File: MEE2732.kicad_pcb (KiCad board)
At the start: 2 copper layers, 16.6 x 32.9 mm, 6 parts, among them J1 Molex 78805 socket 27C32 pino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, SW1 SW_SPDT, U1 28C64

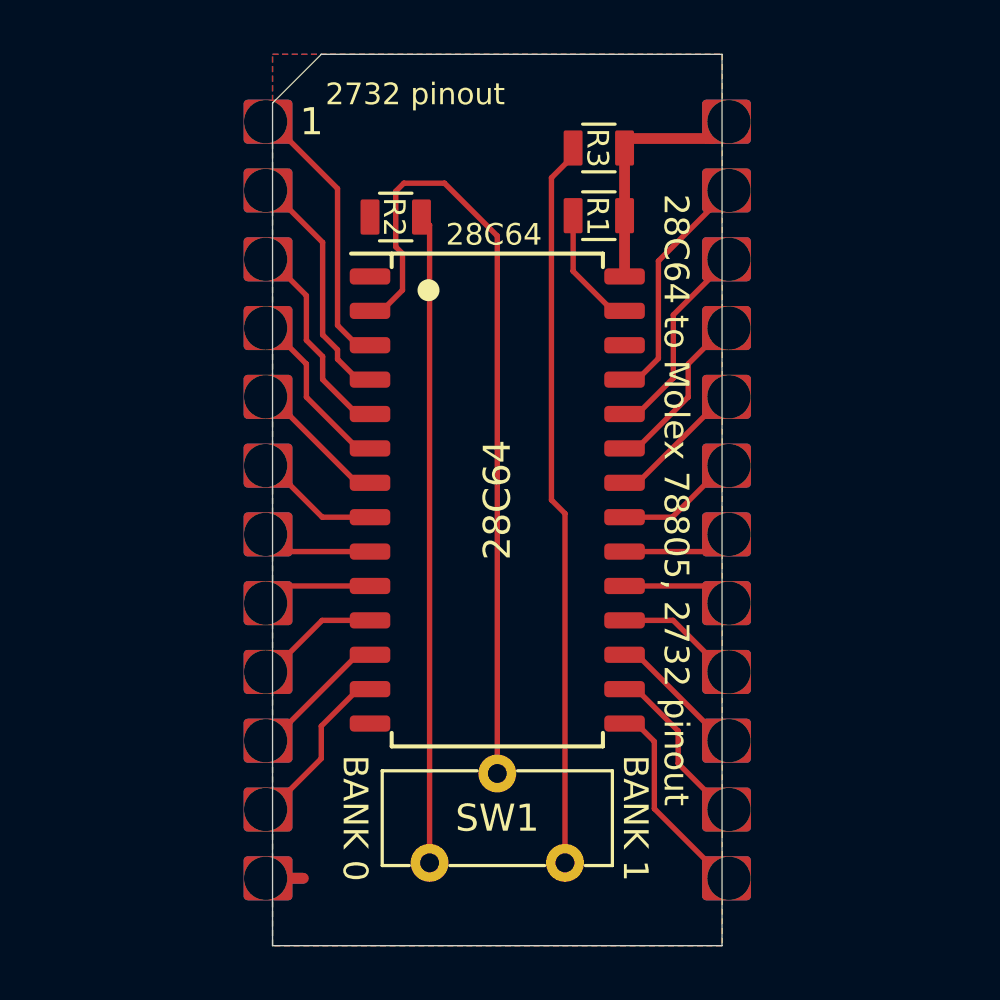
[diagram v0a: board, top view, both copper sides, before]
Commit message: kicad 6, flashopt100 programming socket
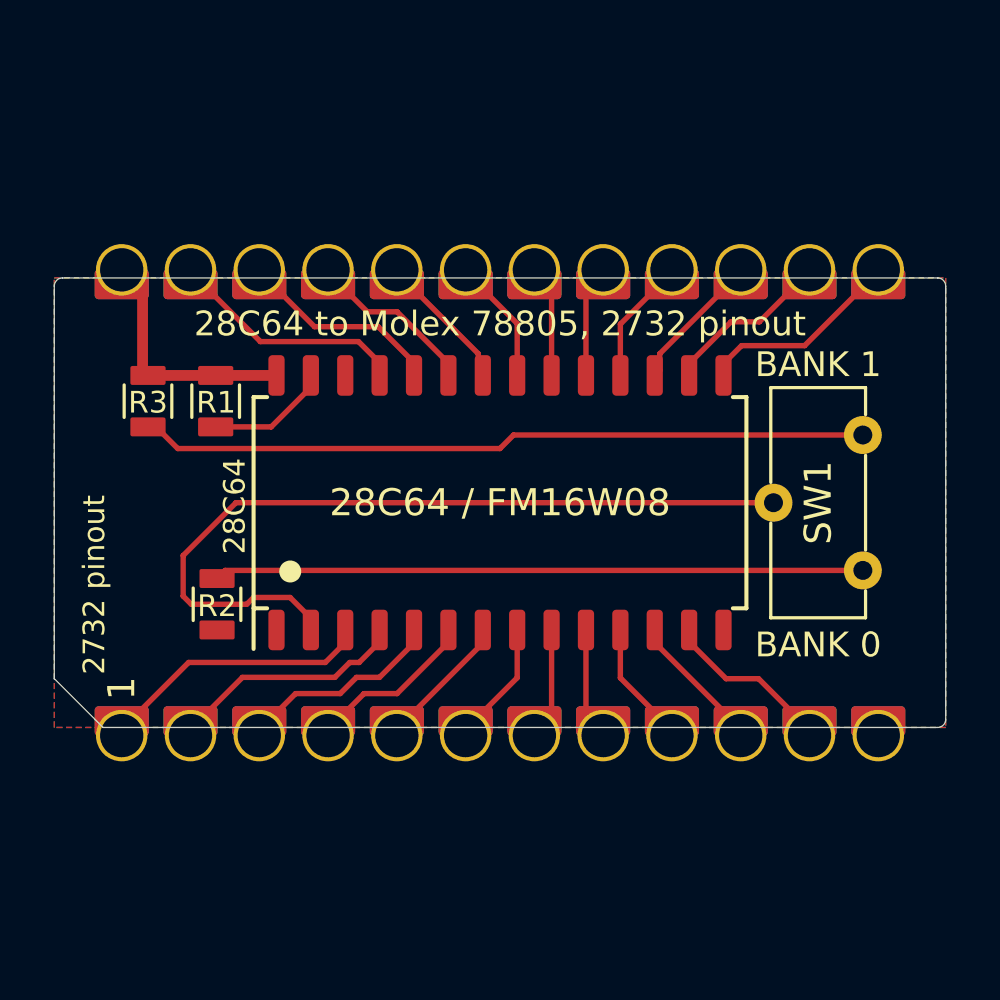
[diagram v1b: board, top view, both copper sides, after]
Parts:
- J1: value Molex 78805 socket 27C32 pinout -> Molex 78805 socket with 27C32 pinout
- U1: value 28C64 -> 28C64 / FM16W08
- moved R3 19.1 mm to (134.3, 95.5), turned to 90 degrees
- moved SW1 16.6 mm to (159.1, 99.3), turned to -90 degrees
- moved R2 15.7 mm to (136.9, 103.0), turned to -90 degrees
- moved R1 15.7 mm to (136.8, 95.5), turned to 90 degrees
- moved J1 0.14 mm to (147.3, 99.3), turned to 90 degrees
- moved U1 0.14 mm to (147.3, 99.3), turned to 90 degrees
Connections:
- net /~CE renamed /~{CE}
- net /~OE renamed /~{OE}
- net /~WE renamed /~{WE}
- U1 pad 1: (no net) -> unconnected-(U1-Pad1)
- U1 pad 26: (no net) -> unconnected-(U1-Pad26)
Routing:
- net GND: track 2.77 -> 0.00 mm
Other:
- board size 16.6 x 32.9 mm -> 32.9 x 16.6 mm
- net class Default removed
- board text added: "${TITLE} ${REVISION} ${COMMENT2}"
- board text added: "R1, R2, R3: ${00000000-0000-0000-0000-00005d22c129:VALUE} SW1: CL-SB-12C-02 or CL-SB-12C-12 Use Carrier: Molex78802_PCB_24 v004"
- board text removed: "Carrier: Molex78802_PCB_24 v004"
- board text removed: "R1, R2, R3: 100k"
- board text removed: "SW1: CL-SB-12C-02 or CL-SB-12C-12"
- board text removed: "github.com/bkw777/Teeprom"

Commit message: MEE2732 minor tidy up
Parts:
- moved R3 3.98 mm to (135.9, 99.2), turned to 180 degrees
- moved R2 1.04 mm to (135.9, 102.6), turned to 180 degrees
- moved R1 0.93 mm to (135.9, 95.8), turned to 180 degrees
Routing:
- net VCC: track 9.05 -> 13.7 mm
- net Net-(R3-Pad1): track 26.9 -> 24.8 mm
- net /A12: track 29.8 -> 30.6 mm
- net /~{WE}: track 4.56 -> 5.19 mm
- net Net-(R2-Pad1): track 24.0 -> 24.5 mm
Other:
- board text removed: "2732 pinout"
- board text removed: "28C64"
